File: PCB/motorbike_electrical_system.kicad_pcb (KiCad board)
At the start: 2 copper layers, 101.9 x 82.9 mm, 72 parts, among them IC2 BDX34C, IC3 BDX34C, K1 RT42xxxx, Q1 D45VH10, Q10 BC337, Q11 BC337, Q12 BC327, Q13 BC337, Q14 D45VH10, Q15 D45VH10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

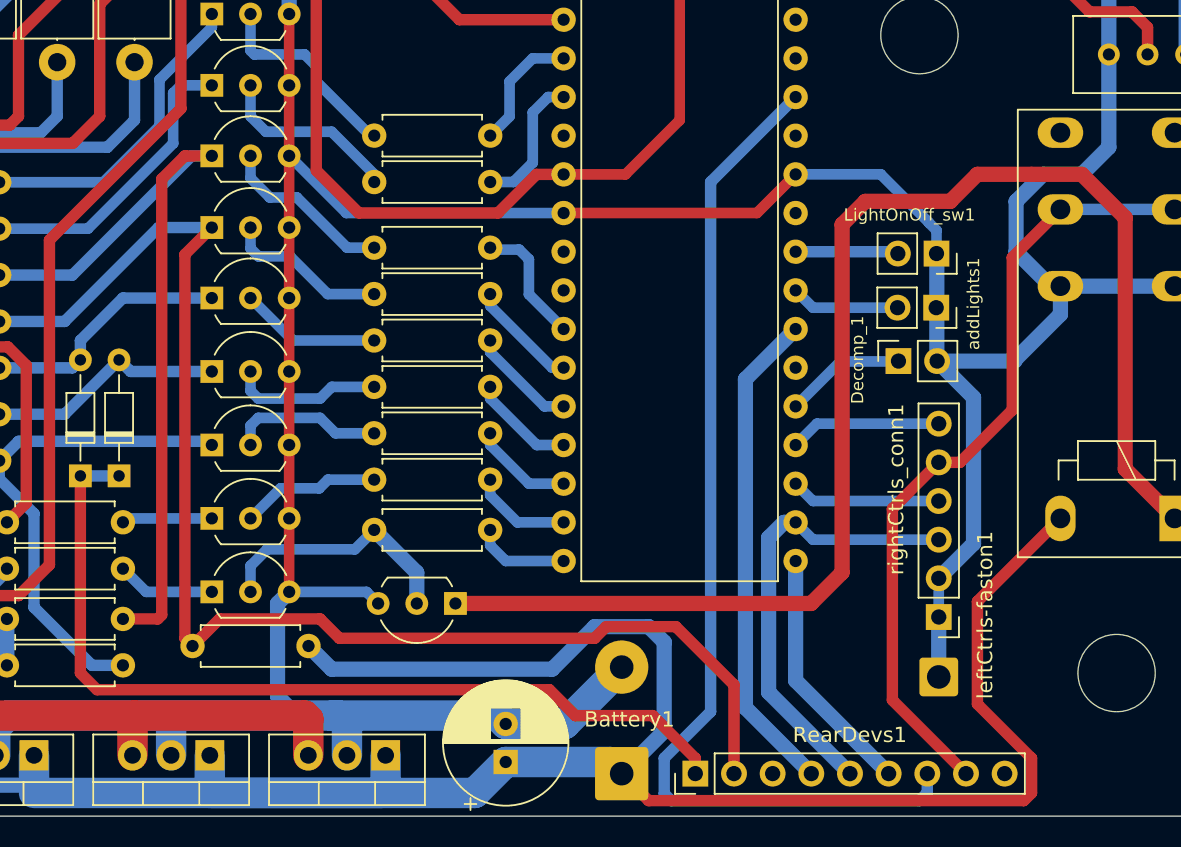
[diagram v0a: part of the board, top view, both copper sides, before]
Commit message: feat: power-off button
Because MCU could have a problem for an unpredictable reason, a power-off button has been added to stop the current to the MCU.
But, because I am paranoide and the transistor could have problems, I connected the power-off button yo the MCU too. In this way
it can always shutdown itself
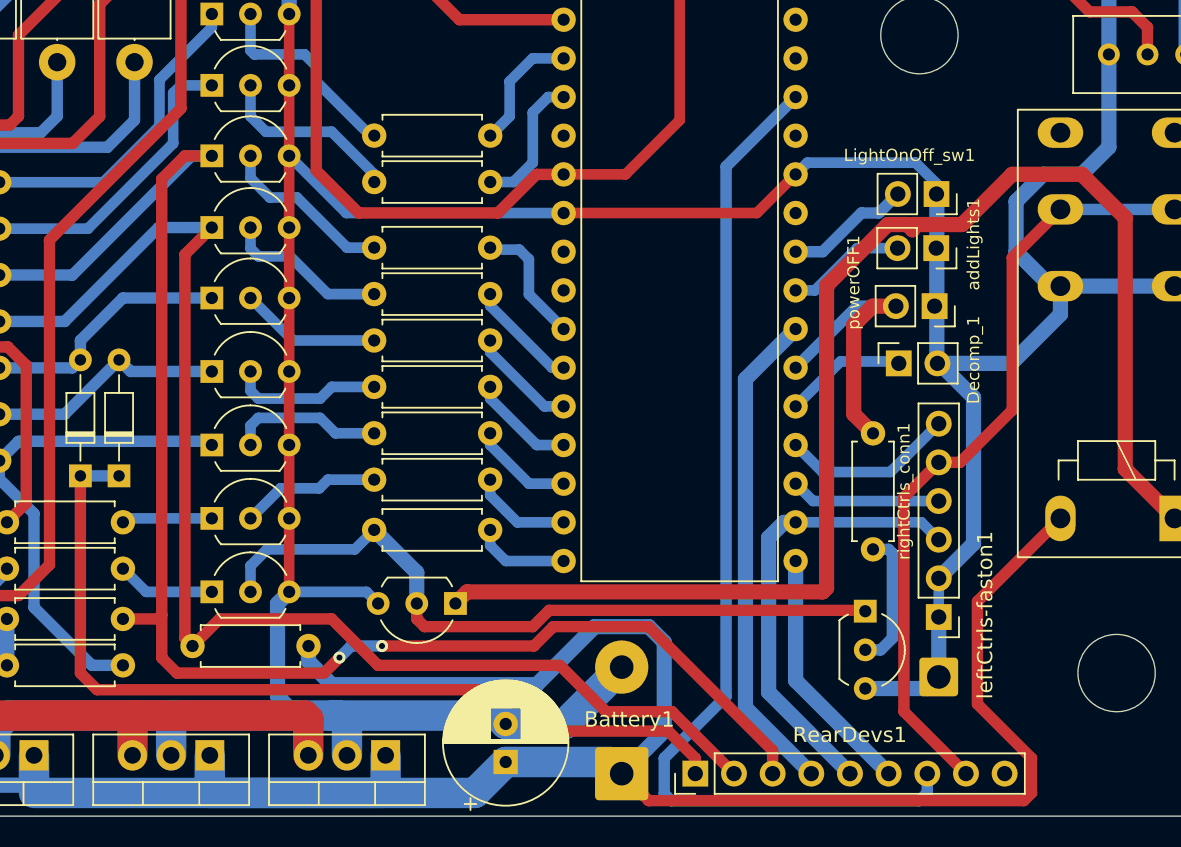
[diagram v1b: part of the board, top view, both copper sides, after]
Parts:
- added Q16: BC337, Package_TO_SOT_THT:TO-92L_Inline_Wide, F.Cu at (187.0, 125.1)
- added RA29: 10K, Resistor_THT:R_Axial_DIN0207_L6.3mm_D2.5mm_P7.62mm_Horizontal, F.Cu at (187.5, 121.0)
- added powerOFF1: Conn_01x02, Connector_PinSocket_2.54mm:PinSocket_1x02_P2.54mm_Vertical, F.Cu at (191.5, 105.1)
- moved addLights1 3.91 mm to (191.6, 101.3)
- moved LightOnOff_sw1 3.91 mm to (191.6, 97.7)
- moved Decomp_1 0.15 mm to (189.2, 108.8)
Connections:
- Q7 pad 1: Net-(Q7-Pad1) -> c_rightArrow
- RA14 pad 1: Net-(Q7-Pad1) -> c_rightArrow
- RA28 pad 2: Net-(Q7-Pad1) -> c_rightArrow
- RA5 pad 1: Net-(Q7-Pad1) -> c_rightArrow
- U4 pad 26: unconnected-(U4-Pad26) -> i_powerOFF
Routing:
- net c_rightArrow: track 0.00 -> 142.5 mm, vias 0 -> 2
- net Net-(Q7-Pad1): track 93.0 -> 0.00 mm
- net Net-(Q11-Pad2): track 16.8 -> 48.0 mm
- net i_powerOFF: track 0.00 -> 19.2 mm
- net GND: track 281.6 -> 293.2 mm
- net Net-(Q16-Pad2): track 0.00 -> 9.06 mm
- net c_leftArrow: track 131.2 -> 127.1 mm
- net i_lightON/OFF: track 6.77 -> 8.29 mm
- net i_engineON: track 9.98 -> 11.5 mm
- net +12V: track 207.3 -> 208.8 mm
- net Net-(K1-PadA1): track 91.3 -> 90.1 mm
- net i_addLight: track 7.17 -> 7.85 mm
- net c_engineOFF: track 52.0 -> 51.3 mm

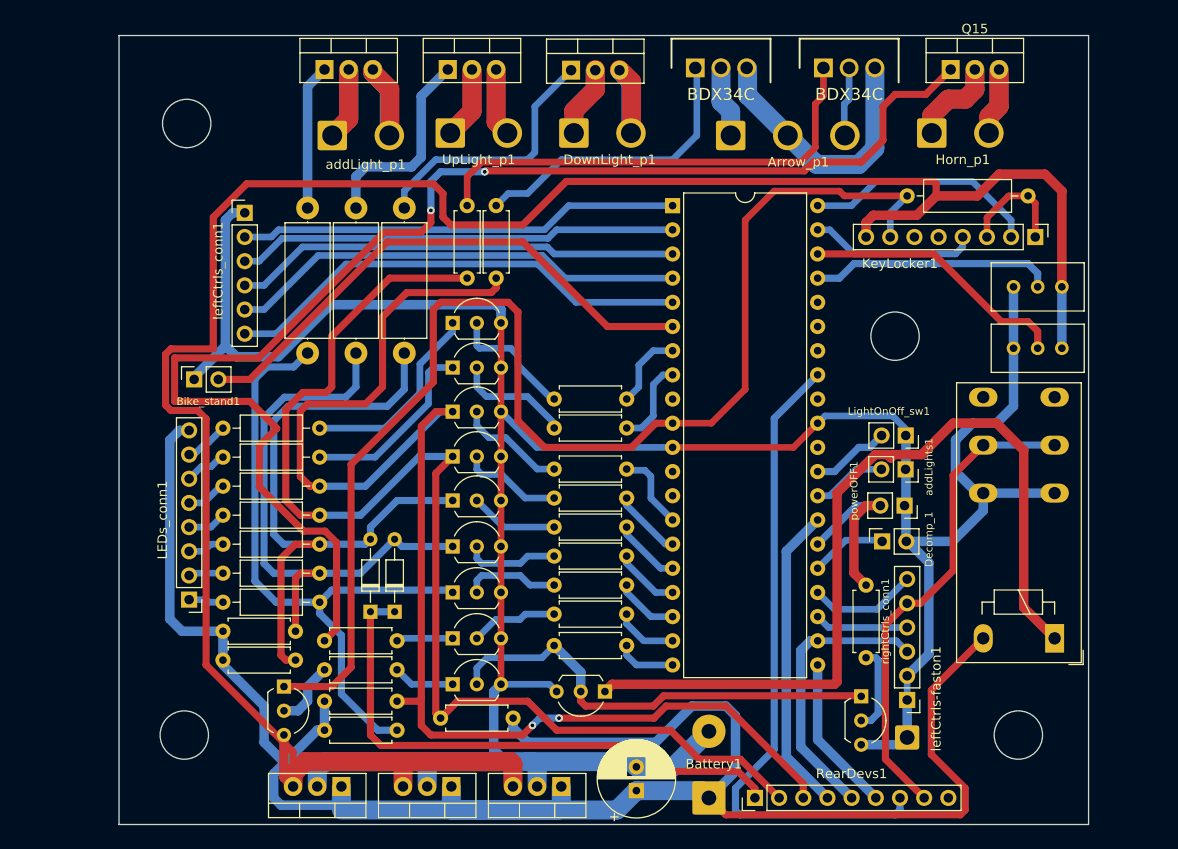
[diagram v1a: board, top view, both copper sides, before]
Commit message: Floating BC337 transistors bases fixed, and PowerOFF button management added
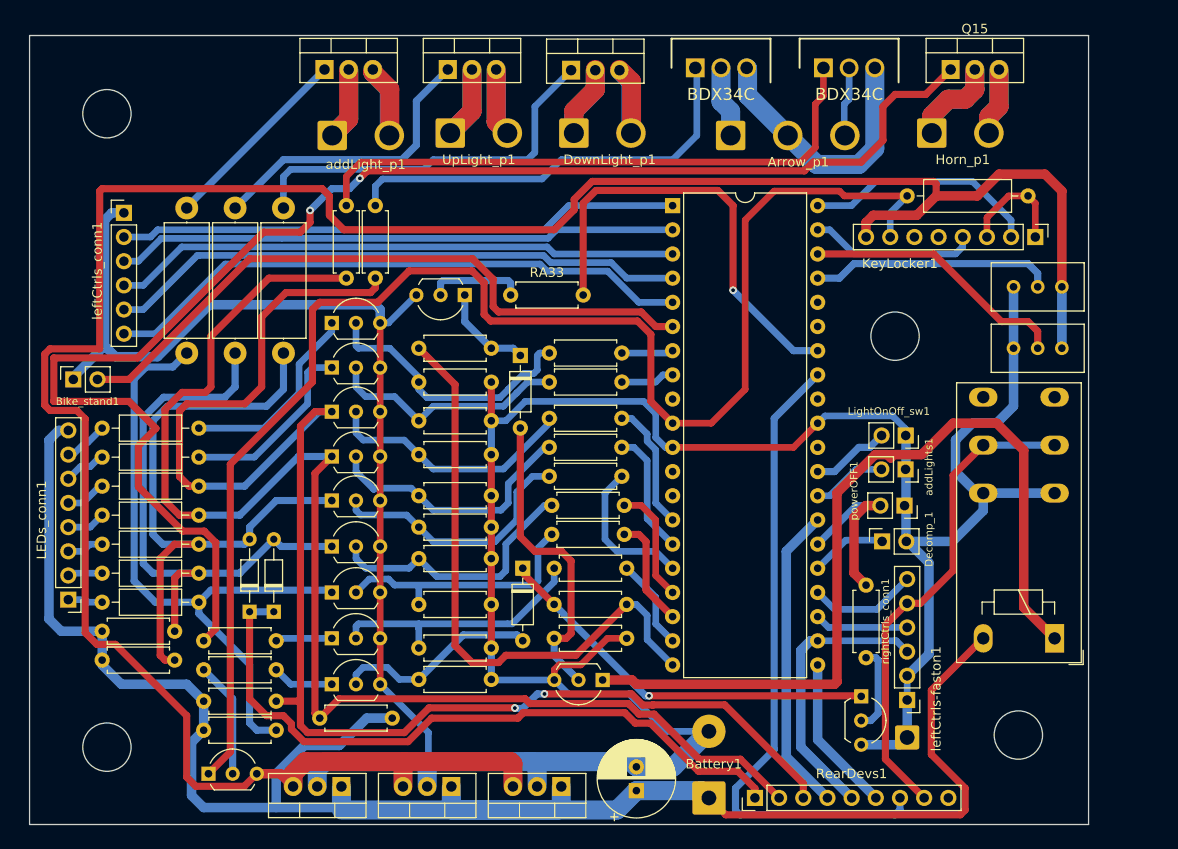
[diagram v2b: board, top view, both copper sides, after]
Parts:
- added D3: 2V, Diode_THT:D_DO-35_SOD27_P7.62mm_Horizontal, F.Cu at (151.1, 89.3)
- added D4: 2V, Diode_THT:D_DO-35_SOD27_P7.62mm_Horizontal, F.Cu at (151.4, 111.6)
- added Q17: BC337, Package_TO_SOT_THT:TO-92L_Inline_Wide, F.Cu at (145.3, 82.9)
- added RA30: 100K, Resistor_THT:R_Axial_DIN0207_L6.3mm_D2.5mm_P7.62mm_Horizontal, F.Cu at (140.5, 123.3)
- added RA31: 100K, Resistor_THT:R_Axial_DIN0207_L6.3mm_D2.5mm_P7.62mm_Horizontal, F.Cu at (154.7, 119.0)
- added RA32: 100K, Resistor_THT:R_Axial_DIN0207_L6.3mm_D2.5mm_P7.62mm_Horizontal, F.Cu at (140.5, 120.0)
- added RA33: 10K, Resistor_THT:R_Axial_DIN0207_L6.3mm_D2.5mm_P7.62mm_Horizontal, F.Cu at (150.1, 82.9)
- added RA34: 100K, Resistor_THT:R_Axial_DIN0207_L6.3mm_D2.5mm_P7.62mm_Horizontal, F.Cu at (140.5, 115.5)
- added RA35: 100K, Resistor_THT:R_Axial_DIN0207_L6.3mm_D2.5mm_P7.62mm_Horizontal, F.Cu at (140.5, 110.6)
- added RA36: 100K, Resistor_THT:R_Axial_DIN0207_L6.3mm_D2.5mm_P7.62mm_Horizontal, F.Cu at (140.5, 107.3)
- added RA37: 100K, Resistor_THT:R_Axial_DIN0207_L6.3mm_D2.5mm_P7.62mm_Horizontal, F.Cu at (140.5, 104.0)
- added RA38: 100K, Resistor_THT:R_Axial_DIN0207_L6.3mm_D2.5mm_P7.62mm_Horizontal, F.Cu at (140.5, 99.7)
- added RA39: 100K, Resistor_THT:R_Axial_DIN0207_L6.3mm_D2.5mm_P7.62mm_Horizontal, F.Cu at (140.5, 96.2)
- added RA40: 100K, Resistor_THT:R_Axial_DIN0207_L6.3mm_D2.5mm_P7.62mm_Horizontal, F.Cu at (140.5, 92.1)
- added RA41: 4K, Resistor_THT:R_Axial_DIN0207_L6.3mm_D2.5mm_P7.62mm_Horizontal, F.Cu at (148.1, 88.5)
- RA8: value 3K -> 4K
- moved Q10 12.7 mm to (131.3, 85.9)
- moved Q11 12.7 mm to (131.3, 123.8)
- moved Q3 12.7 mm to (131.3, 114.2)
- moved Q4 12.7 mm to (131.3, 109.4)
- moved Q5 12.7 mm to (131.3, 104.5)
- moved Q6 12.7 mm to (131.3, 99.9)
- moved Q7 12.7 mm to (131.3, 95.2)
- moved Q8 12.7 mm to (131.3, 90.6)
- moved Q9 12.7 mm to (131.3, 119.0)
- moved RA13 12.7 mm to (132.9, 81.2)
- moved RA14 12.7 mm to (135.9, 81.2)
- moved D2 12.7 mm to (125.2, 116.2)
- moved LEDs_conn1 12.7 mm to (103.6, 115.0)
- moved RA1 12.7 mm to (117.4, 115.2)
- moved RA10 12.7 mm to (116.1, 89.0)
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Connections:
- Q13 pad 2: Net-(Q11-Pad2) -> Net-(Q13-Pad2)
- Q16 pad 1: Net-(Q11-Pad2) -> Net-(Q16-Pad1)
- RA8 pad 1: Net-(Q11-Pad2) -> Net-(Q16-Pad1)
- U4 pad 34: unconnected-(U4-Pad34) -> o_engineOFF
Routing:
- net GND: track 293.2 -> 363.5 mm
- net o_keepAlive: track 6.27 -> 63.1 mm
- net o_engineOFF: track 0.00 -> 47.0 mm, vias 0 -> 1
- net Net-(Q16-Pad1): track 0.00 -> 40.9 mm, vias 0 -> 1
- net Net-(Q13-Pad2): track 0.00 -> 32.9 mm
- net Net-(Q11-Pad2): track 48.0 -> 21.6 mm
- net +5V: track 233.0 -> 255.3 mm
- net Net-(Q9-Pad2): track 9.18 -> 28.0 mm
- net Net-(Q4-Pad2): track 9.92 -> 28.2 mm
- net Net-(Q5-Pad2): track 9.28 -> 27.3 mm
- net Net-(Q3-Pad2): track 10.0 -> 27.4 mm
- net tempPower: track 139.0 -> 155.9 mm
- net Net-(Q6-Pad2): track 10.7 -> 27.6 mm
- net Net-(Q7-Pad2): track 11.5 -> 26.8 mm
- net Net-(Q10-Pad2): track 13.4 -> 28.6 mm
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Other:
- board size 101.9 x 82.9 mm -> 111.3 x 82.9 mm

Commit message: - Other floating BC337 transistors bases fixed - USB port missing fixed - Small enhancements
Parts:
- removed D1, D2: DIODE, Diode_THT:D_DO-34_SOD68_P7.62mm_Horizontal
- added C1: 1.5m, Capacitor_THT:CP_Radial_D8.0mm_P2.50mm, F.Cu at (123.1, 112.9)
- added RA42: 100K, Resistor_THT:R_Axial_DIN0207_L6.3mm_D2.5mm_P7.62mm_Horizontal, F.Cu at (115.6, 134.5)
- added RA43: 100K, Resistor_THT:R_Axial_DIN0207_L6.3mm_D2.5mm_P7.62mm_Horizontal, F.Cu at (141.2, 128.2)
- added RA44: 100K, Resistor_THT:R_Axial_DIN0207_L6.3mm_D2.5mm_P7.62mm_Horizontal, F.Cu at (153.7, 127.9)
- added USB-5V1: Conn_01x01, Connector_Wire:SolderWire-1.5sqmm_1x01_D1.7mm_OD3.9mm, F.Cu at (102.4, 121.6)
- moved RA15 0.50 mm to (126.0, 119.3)
- moved RA24 0.50 mm to (118.4, 128.7)
- moved RA28 0.50 mm to (118.4, 125.6)
- moved RA7 0.50 mm to (126.0, 122.3)
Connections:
- RearDevs1 pad 1: c_rearLight -> i_lightON/OFF
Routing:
- net c_rearLight: track 72.5 -> 0.00 mm
- net Net-(Q17-Pad2): track 10.1 -> 58.7 mm, vias 0 -> 1
- net i_lightON/OFF: track 8.29 -> 46.3 mm
- net GND: track 363.5 -> 400.5 mm
- net +5V: track 255.3 -> 291.8 mm
- net Net-(Q16-Pad2): track 9.06 -> 36.2 mm
- net c_leftArrow: track 140.0 -> 149.4 mm
- net Net-(Q15-Pad1): track 154.4 -> 163.3 mm
- net Net-(Q3-Pad1): track 68.2 -> 65.5 mm
- net Net-(Q13-Pad1): track 90.2 -> 92.6 mm
- net +12V: track 196.0 -> 197.5 mm
- net c_rightArrow: track 156.1 -> 157.1 mm
- net Net-(Q4-Pad1): track 60.2 -> 59.6 mm
- net Net-(Q9-Pad1): track 5.95 -> 5.44 mm
- net Net-(Q11-Pad1): track 6.47 -> 5.97 mm
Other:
- outline, holes or cut-outs redrawn

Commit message: External cockpit power-connector added and wrong transistor type fixed
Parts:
- added Q18: BC327, Package_TO_SOT_THT:TO-92L_Inline_Wide, F.Cu at (187.7, 126.9)
- added Q19: BC327, Package_TO_SOT_THT:TO-92L_Inline_Wide, F.Cu at (201.9, 122.3)
- added Q20: BC327, Package_TO_SOT_THT:TO-92L_Inline_Wide, F.Cu at (214.4, 121.3)
- added RA45: 10K, Resistor_THT:R_Axial_DIN0207_L6.3mm_D2.5mm_P7.62mm_Horizontal, F.Cu at (176.0, 128.2)
- added RA46: 3K, Resistor_THT:R_Axial_DIN0207_L6.3mm_D2.5mm_P7.62mm_Horizontal, F.Cu at (212.1, 107.3)
- added RA47: 3K, Resistor_THT:R_Axial_DIN0207_L6.3mm_D2.5mm_P7.62mm_Horizontal, F.Cu at (212.1, 118.0)
- added koso-1: Conn_01x03, Connector_PinHeader_2.54mm:PinHeader_1x03_P2.54mm_Vertical, F.Cu at (214.4, 136.8)
- C1: value 1.5m -> 1500uF
- moved Q16 6.31 mm to (191.0, 129.9), turned to 180 degrees
- moved K1 2.58 mm to (207.3, 116.4)
- moved RV1 2.53 mm to (206.5, 86.5)
- moved leftCtrls-faston1 2.50 mm to (194.1, 130.4)
- moved RV2 2.09 mm to (206.5, 80.7)
- moved RA29 1.52 mm to (187.5, 119.5)
- moved KeyLocker1 1.27 mm to (205.2, 75.6)
- moved R1 1.02 mm to (191.8, 71.5)
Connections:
- net i_lightON/OFF renamed c_rearLight
- D4 pad 1: Net-(Q16-Pad1) -> Net-(D4-Pad1)
- RA29 pad 1: Net-(Q16-Pad2) -> Net-(RA29-Pad1)
- RA44 pad 1: GND -> +5V
- RA44 pad 2: Net-(Q16-Pad2) -> Net-(RA29-Pad1)
- RA8 pad 1: Net-(Q16-Pad1) -> Net-(D4-Pad1)
- U4 pad 26: i_powerOFF -> unconnected-(U4-Pad26)
- U4 pad 30: unconnected-(U4-Pad30) -> tempPower
- U4 pad 9: unconnected-(U4-Pad9) -> i_powerOFF
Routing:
- net i_powerOFF: track 19.2 -> 116.6 mm, vias 0 -> 1
- net Net-(D4-Pad1): track 0.00 -> 55.6 mm, vias 0 -> 1
- net GND: track 400.5 -> 445.8 mm
- net +12V: track 197.5 -> 235.9 mm, vias 0 -> 1
- net Net-(RA29-Pad1): track 0.00 -> 34.9 mm
- net Net-(Q19-Pad1): track 0.00 -> 31.1 mm
- net Net-(Q16-Pad2): track 36.2 -> 5.93 mm
- net Net-(Q19-Pad2): track 0.00 -> 21.1 mm
- net tempPower: track 155.9 -> 166.8 mm, vias 0 -> 1
- net Net-(Q16-Pad1): track 40.9 -> 48.3 mm, vias 1 -> 0
- net +5V: track 291.8 -> 297.5 mm, vias 0 -> 1
- net Net-(Q20-Pad2): track 0.00 -> 3.41 mm
- net c_engineOFF: track 51.3 -> 54.1 mm
- net Net-(RV1-Pad2): track 28.3 -> 25.7 mm
- net i_Vx1: track 24.8 -> 27.2 mm
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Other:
- board size 111.3 x 82.9 mm -> 116.9 x 83.4 mm

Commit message: Fixes and optimizations (unuseful I/O lines dropped)
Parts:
- added RA48: 100K, Resistor_THT:R_Axial_DIN0207_L6.3mm_D2.5mm_P7.62mm_Horizontal, F.Cu at (165.4, 125.1)
- added RA49: 100K, Resistor_THT:R_Axial_DIN0207_L6.3mm_D2.5mm_P7.62mm_Horizontal, F.Cu at (212.1, 96.9)
- C1: value 1500uF -> C_Polarized_Small
- RearDevs1: value Conn_01x09 -> Conn_01x08; footprint Connector_PinHeader_2.54mm:PinHeader_1x09_P2.54mm_Vertical -> Connector_PinHeader_2.54mm:PinHeader_1x08_P2.54mm_Vertical
- moved Q13 4.32 mm to (155.5, 123.4)
- moved RA44 1.37 mm to (152.4, 128.4)
- moved RA43 1.08 mm to (140.5, 127.4)
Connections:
- RearDevs1 pad 4: o_stopLight -> unconnected-(RearDevs1-Pad4)
- RearDevs1 pad 5: i_brakeSwitch -> c_brakeSwitch
- U4 pad 22: i_brakeSwitch -> unconnected-(U4-Pad22)
- U4 pad 27: o_stopLight -> unconnected-(U4-Pad27)
- rightCtrls_conn1 pad 3: i_brakeSwitch -> c_brakeSwitch
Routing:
- net +12V: track 235.9 -> 272.1 mm, vias 1 -> 2
- net o_stopLight: track 31.7 -> 0.00 mm
- net i_brakeSwitch: track 31.1 -> 0.00 mm
- net c_brakeSwitch: track 0.00 -> 28.5 mm, vias 0 -> 1
- net GND: track 445.8 -> 460.5 mm
- net Net-(K1-PadA1): track 94.3 -> 99.3 mm
- net o_startEngine: track 18.4 -> 21.4 mm
- net Net-(Q16-Pad1): track 48.3 -> 51.1 mm
- net c_rightArrow: track 157.1 -> 154.7 mm
- net Net-(Q18-Pad2): track 34.9 -> 36.3 mm
- net Net-(Q17-Pad2): track 58.7 -> 57.7 mm
- net Net-(D4-Pad1): track 55.6 -> 54.9 mm
- net +5V: track 297.5 -> 298.2 mm

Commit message: fixes...
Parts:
- added C2: 100nF, Capacitor_THT:C_Disc_D4.3mm_W1.9mm_P5.00mm, F.Cu at (198.4, 86.2)
- R1: value 500 -> 1K; footprint Resistor_THT:R_Axial_DIN0309_L9.0mm_D3.2mm_P12.70mm_Horizontal -> Resistor_THT:R_Axial_DIN0207_L6.3mm_D2.5mm_P10.16mm_Horizontal
- moved RV2 1.27 mm to (207.8, 80.7)
- moved RV1 1.27 mm to (207.8, 86.5)
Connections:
- U4 pad 30: tempPower -> unconnected-(U4-Pad30)
- U4 pad 32: unconnected-(U4-Pad32) -> +5V
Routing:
- net +5V: track 298.2 -> 328.2 mm
- net tempPower: track 166.8 -> 155.1 mm, vias 1 -> 0
- net GND: track 460.5 -> 466.3 mm
- net Net-(RV1-Pad2): track 25.7 -> 30.4 mm
- net Net-(Q1-Pad1): track 20.5 -> 23.4 mm
- net i_powerOFF: track 116.6 -> 114.1 mm
- net i_Vx1: track 27.2 -> 24.9 mm
- net Net-(RV2-Pad2): track 23.5 -> 25.5 mm
- net c_leftArrow: track 149.8 -> 151.4 mm
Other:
- outline, holes or cut-outs redrawn
